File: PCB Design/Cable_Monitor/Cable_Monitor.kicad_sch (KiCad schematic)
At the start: 57 parts, among them J1 USB_B_Micro, P1 ${SIM.PARAMS}, P2 ${SIM.PARAMS}, Q1 BSS316N, SW1 On / Off Button, U1 SiP32508, U2 LD1117S33TR, U3 DRV5053_THT, U4 DRV5053_THT

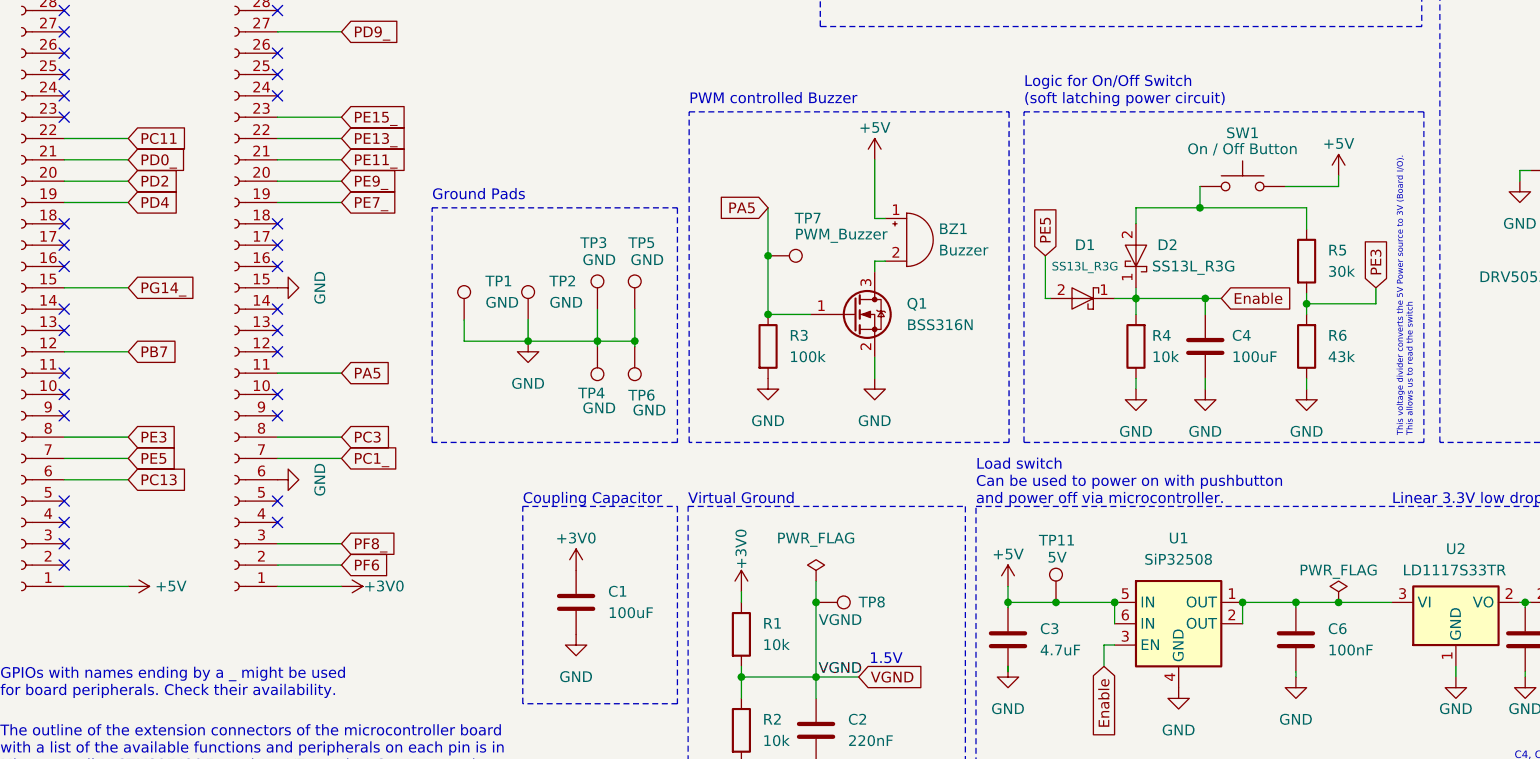
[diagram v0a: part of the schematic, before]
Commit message: Schematics Update and measurement Demo
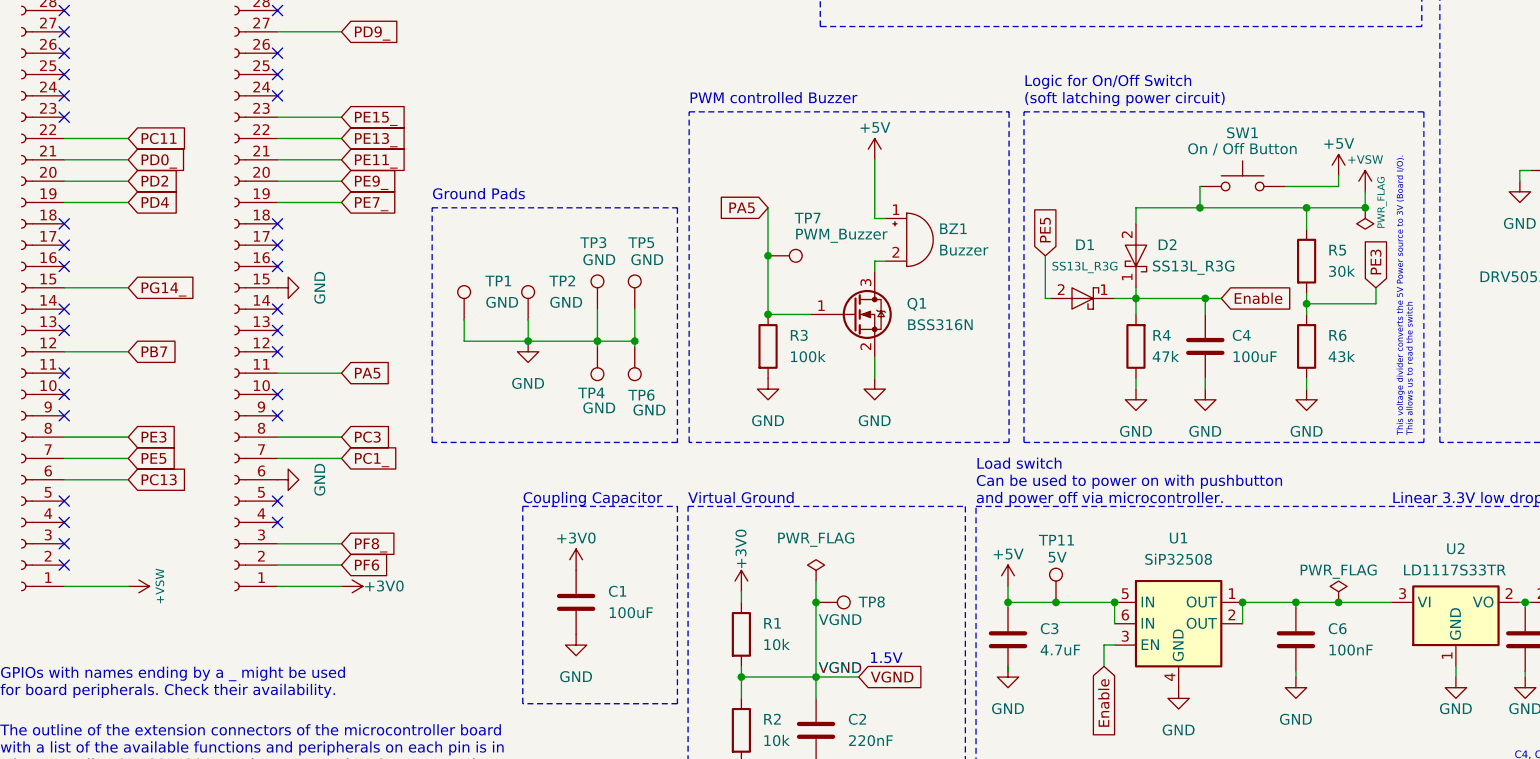
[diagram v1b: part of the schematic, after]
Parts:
- R4: value 10k -> 47k
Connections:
- net +5V: no longer P1.1 (Pin_1)
- net +VSW: now reaches D2.2 (A), R5.1, SW1.1
- net +VSW: now also P1.1 (Pin_1)
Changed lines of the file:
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@@
     (title "Cable Monitor")
     (date "2023-09-29")
-    (rev "V.1.0")
+    (rev "V.1.1")
     (company "ZHAW")
     (comment 1 "Created by: horvaale & weytim01")
     (comment 2 "This is the Hardware Schematic of the Cable Monitor PCB which was designed for ET.PM3")
+    (comment 3 "V.1.1 Fixed 5V supply for MCU. Changed R4 value to 47k")
   )
   (junction (at 158.115 164.465) (diameter 0) (color 0 0 0 0)
@@
   (junction (at 173.355 127.635) (diameter 0) (color 0 0 0 0)
   )
+  (junction (at 169.545 80.645) (diameter 0) (color 0 0 0 0)
+  )
   (junction (at 102.235 136.525) (diameter 0) (color 0 0 0 0)
   )
@@
   (junction (at 161.925 127.635) (diameter 0) (color 0 0 0 0)
   )
+  (junction (at 176.53 80.645) (diameter 0) (color 0 0 0 0)
+  )
   (junction (at 133.985 127.635) (diameter 0) (color 0 0 0 0)
   )
@@
     (stroke (width 0) (type default))
   )
+  (wire (pts (xy 169.545 80.645) (xy 176.53 80.645))
+    (stroke (width 0) (type default))
+  )
   (wire (pts (xy 147.955 180.975) (xy 158.115 180.975))
     (stroke (width 0) (type default))
@@
     (stroke (width 0) (type default))
   )
+  (wire (pts (xy 176.53 78.74) (xy 176.53 80.645))
+    (stroke (width 0) (type default))
+  )
   (wire (pts (xy 222.885 122.555) (xy 222.885 124.46))
     (stroke (width 0) (type default))
@@
     )
   )
+  (symbol (lib_id "power:+VSW") (at 176.53 78.74 0) (unit 1)
+    (in_bom yes) (on_board yes) (dnp no)
+    (property "Reference" "#PWR051" (at 176.53 82.55 0)
+      (effects (font (size 1.27 1.27)) hide)
+    )
+    (property "Value" "+VSW" (at 176.53 74.93 0)
+      (effects (font (size 1 1)))
+    )
+    (property "Footprint" "" (at 176.53 78.74 0)
+      (effects (font (size 1.27 1.27)) hide)
+    )
+    (property "Datasheet" "" (at 176.53 78.74 0)
+      (effects (font (size 1.27 1.27)) hide)
+    )
+    (pin "1")
+    (instances
+      (project "Cable_Monitor"
+        (path "/1f276d59-ad9b-4e70-a842-f3b7e562eb9b"
+          (reference "#PWR051") (unit 1)
+        )
+      )
+    )
+  )
   (symbol (lib_id "Connector:TestPoint") (at 220.345 85.09 0) (unit 1)
     (in_bom yes) (on_board yes) (dnp no)
@@
     )
   )
+  (symbol (lib_id "power:PWR_FLAG") (at 176.53 80.645 180) (unit 1)
+    (in_bom yes) (on_board yes) (dnp no)
+    (property "Reference" "#FLG05" (at 176.53 82.55 0)
+      (effects (font (size 1.27 1.27)) hide)
+    )
+    (property "Value" "PWR_FLAG" (at 178.435 80.01 90)
+      (effects (font (size 0.85 0.85)))
+    )
+    (property "Footprint" "" (at 176.53 80.645 0)
+      (effects (font (size 1.27 1.27)) hide)
+    )
+    (property "Datasheet" "~" (at 176.53 80.645 0)
+      (effects (font (size 1.27 1.27)) hide)
+    )
+    (pin "1")
+    (instances
+      (project "Cable_Monitor"
+        (path "/1f276d59-ad9b-4e70-a842-f3b7e562eb9b"
+          (reference "#FLG05") (unit 1)
+        )
+      )
+    )
+  )
   (symbol (lib_id "Connector:TestPoint") (at 89.535 92.71 0) (unit 1)
     (in_bom yes) (on_board yes) (dnp no)
@@
     )
   )
+  (symbol (lib_id "power:+VSW") (at 29.21 125.73 270) (unit 1)
+    (in_bom yes) (on_board yes) (dnp no)
+    (property "Reference" "#PWR052" (at 25.4 125.73 0)
+      (effects (font (size 1.27 1.27)) hide)
+    )
+    (property "Value" "+VSW" (at 33.02 125.73 0)
+      (effects (font (size 1 1)))
+    )
+    (property "Footprint" "" (at 29.21 125.73 0)
+      (effects (font (size 1.27 1.27)) hide)
+    )
+    (property "Datasheet" "" (at 29.21 125.73 0)
+      (effects (font (size 1.27 1.27)) hide)
+    )
+    (pin "1")
+    (instances
+      (project "Cable_Monitor"
+        (path "/1f276d59-ad9b-4e70-a842-f3b7e562eb9b"
+          (reference "#PWR052") (unit 1)
+        )
+      )
+    )
+  )
   (symbol (lib_id "power:GND") (at 46.99 113.03 90) (unit 1)
     (in_bom yes) (on_board yes) (dnp no) (fields_autoplaced)
@@
       (effects (font (size 1.27 1.27)) (justify right))
     )
-    (property "Value" "10k" (at 151.13 98.425 0)
+    (property "Value" "47k" (at 151.13 98.425 0)
       (effects (font (size 1.27 1.27)) (justify right))
     )
@@
         )
       )
-    )
-  )
-  (symbol (lib_id "power:+5V") (at 29.21 125.73 270) (unit 1)
-    (in_bom yes) (on_board yes) (dnp no)
-    (property "Reference" "#PWR02" (at 25.4 125.73 0)
-      (effects (font (size 1.27 1.27)) hide)
-    )
-    (property "Value" "+5V" (at 34.29 125.73 90)
-      (effects (font (size 1.27 1.27)))
-    )
-    (property "Footprint" "" (at 29.21 125.73 0)
-      (effects (font (size 1.27 1.27)) hide)
-    )
-    (property "Datasheet" "" (at 29.21 125.73 0)
-      (effects (font (size 1.27 1.27)) hide)
-    )
-    (pin "1")
-    (instances
-      (project "Cable_Monitor"
-        (path "/1f276d59-ad9b-4e70-a842-f3b7e562eb9b"
-          (reference "#PWR02") (unit 1)
-        )
-      )
